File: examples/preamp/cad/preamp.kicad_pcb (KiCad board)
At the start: 2 copper layers, 52 parts, among them CON1 AVR-ISP-10, J1 CONN_01X02, J2 Conn_01x04, J3 CONN_01X03, J4 CONN_01X02, J5 CONN_01X03, J6 CONN_01X07, J7 CONN_01X02, J8 CONN_01X08, J9 CONN_01X08, Q1 ., SW1 Rotary_Encoder, SW2 SW_Push_Dual, SW3 SW_Push_Dual, SW4 SW_Push_Dual, SW5 SW_Push_Dual, U1 ATMEGA8A-PU, U2 DS1307+, U3 LM7809CT, U4 TDA7313, Y1 Crystal

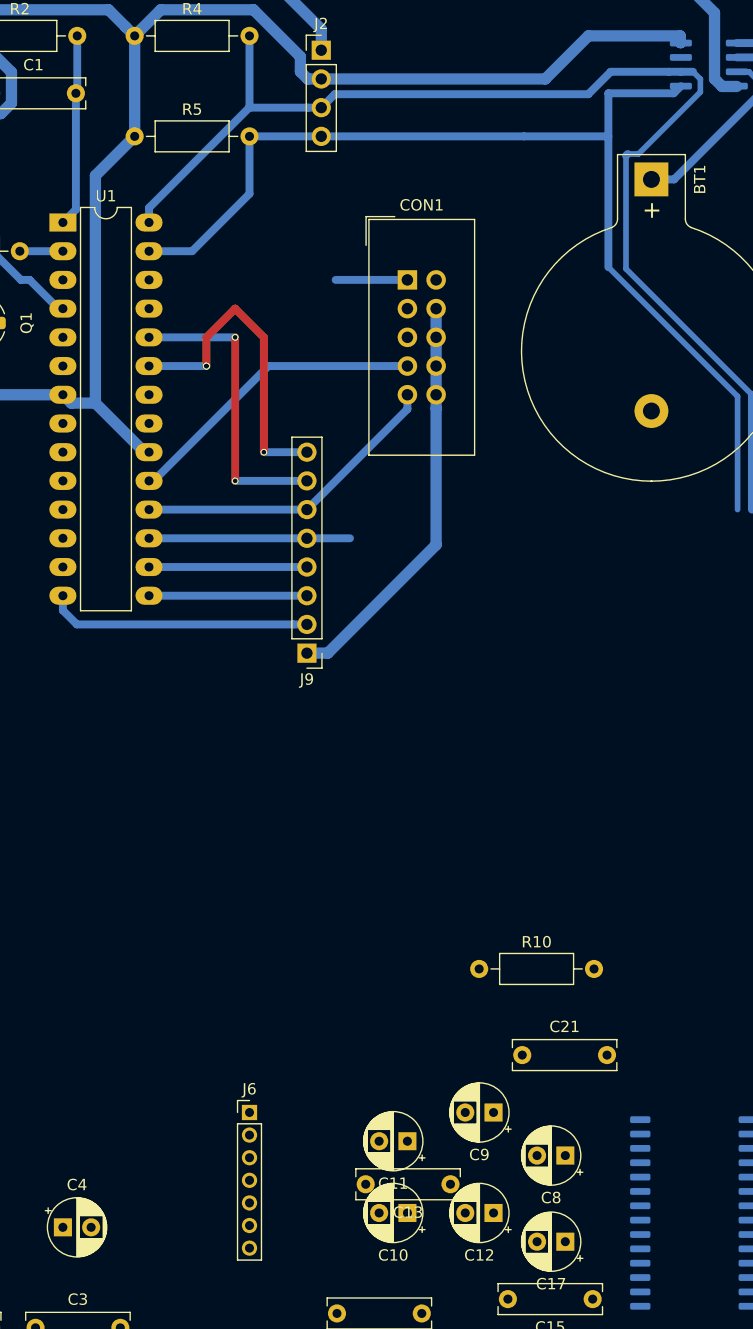
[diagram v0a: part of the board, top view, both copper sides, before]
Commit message: Rename kicad project
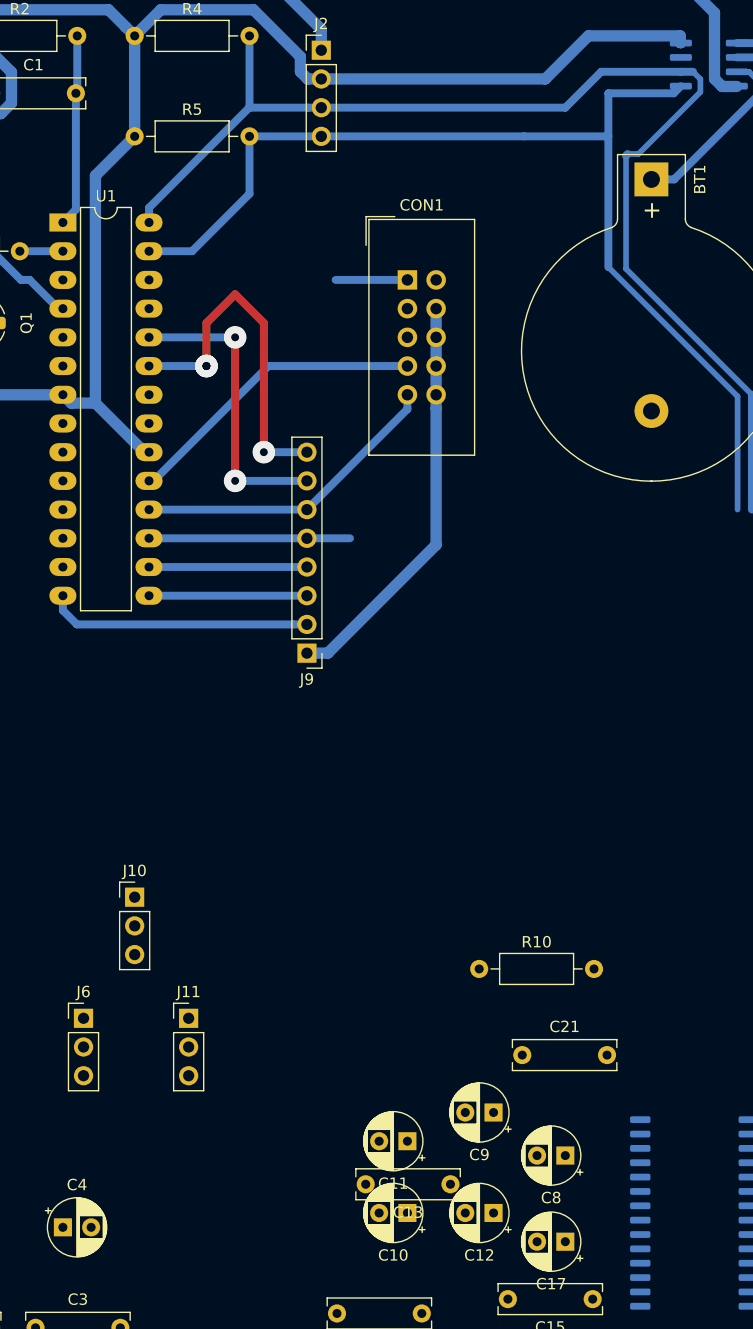
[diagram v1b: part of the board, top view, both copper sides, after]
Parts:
- added J10: Conn_01x03, Connector_PinHeader_2.54mm:PinHeader_1x03_P2.54mm_Vertical, F.Cu at (48.3, 96.5)
- added J11: Conn_01x03, Connector_PinHeader_2.54mm:PinHeader_1x03_P2.54mm_Vertical, F.Cu at (53.0, 107.2)
- J6: value CONN_01X07 -> Conn_01x03; footprint Connector_PinHeader_2.00mm:PinHeader_1x07_P2.00mm_Vertical -> Connector_PinHeader_2.54mm:PinHeader_1x03_P2.54mm_Vertical
- moved J6 16.9 mm to (43.7, 107.2)
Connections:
- J6 pad 2: Net-(C12-Pad2) -> Net-(C8-Pad2)
- J6 pad 3: Net-(C11-Pad2) -> Net-(C7-Pad2)
- U1 pad 25: Net-(U1-Pad25) -> /LEFT
- U1 pad 26: Net-(U1-Pad26) -> /RIGHT
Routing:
- net /ENC0: track 28.8 -> 31.3 mm
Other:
- net class Default: via_dia 0.6 -> 2; via_drill 0.4 -> 0.7
- net class power: via_dia 1 -> 2; via_drill 0.4 -> 0.7

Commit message: Update kicad project
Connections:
- U1 pad 11: Net-(U1-Pad11) -> /ENC1
- U1 pad 23: /ENC0 -> Net-(U1-Pad23)
- U1 pad 24: /ENC1 -> Net-(U1-Pad24)
- U1 pad 6: Net-(U1-Pad6) -> /ENC0
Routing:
- net /ENC0: track 31.3 -> 0.00 mm, vias 3 -> 0
- net /ENC1: track 26.7 -> 0.00 mm, vias 2 -> 0
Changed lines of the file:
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@@
     (thickness 1.6)
     (drawings 0)
-    (tracks 164)
+    (tracks 142)
     (zones 0)
     (modules 54)
@@
   (net 60 "Net-(U1-Pad3)")
   (net 61 "Net-(U1-Pad5)")
-  (net 62 "Net-(U1-Pad6)")
-  (net 63 "Net-(U1-Pad9)")
-  (net 64 "Net-(U1-Pad10)")
-  (net 65 "Net-(U1-Pad11)")
-  (net 66 "Net-(U1-Pad12)")
-  (net 67 "Net-(U1-Pad13)")
-  (net 68 "Net-(U2-Pad1)")
-  (net 69 "Net-(U2-Pad2)")
-  (net 70 "Net-(U2-Pad7)")
-  (net 71 "Net-(U4-Pad22)")
-  (net 72 "Net-(U4-Pad23)")
+  (net 62 "Net-(U1-Pad9)")
+  (net 63 "Net-(U1-Pad10)")
+  (net 64 "Net-(U1-Pad12)")
+  (net 65 "Net-(U1-Pad13)")
+  (net 66 "Net-(U2-Pad1)")
+  (net 67 "Net-(U2-Pad2)")
+  (net 68 "Net-(U2-Pad7)")
+  (net 69 "Net-(U4-Pad22)")
+  (net 70 "Net-(U4-Pad23)")
+  (net 71 "Net-(U1-Pad23)")
+  (net 72 "Net-(U1-Pad24)")
   (net_class Default "Это класс цепей по умолчанию."
     (clearance 0.5)
@@
     (add_net "Net-(Q1-Pad1)")
     (add_net "Net-(U1-Pad10)")
-    (add_net "Net-(U1-Pad11)")
     (add_net "Net-(U1-Pad12)")
     (add_net "Net-(U1-Pad13)")
+    (add_net "Net-(U1-Pad23)")
+    (add_net "Net-(U1-Pad24)")
     (add_net "Net-(U1-Pad3)")
     (add_net "Net-(U1-Pad5)")
-    (add_net "Net-(U1-Pad6)")
     (add_net "Net-(U1-Pad9)")
     (add_net "Net-(U2-Pad1)")
@@
     )
     (pad 1 smd roundrect (at -2.475 1.905 180) (size 1.95 0.6) (layers B.Cu B.Paste B.Mask) (roundrect_rratio 0.25)
-      (net 68 "Net-(U2-Pad1)"))
+      (net 66 "Net-(U2-Pad1)"))
     (pad 2 smd roundrect (at -2.475 0.635 180) (size 1.95 0.6) (layers B.Cu B.Paste B.Mask) (roundrect_rratio 0.25)
-      (net 69 "Net-(U2-Pad2)"))
+      (net 67 "Net-(U2-Pad2)"))
     (pad 3 smd roundrect (at -2.475 -0.635 180) (size 1.95 0.6) (layers B.Cu B.Paste B.Mask) (roundrect_rratio 0.25)
       (net 1 "Net-(BT1-Pad1)"))
@@
       (net 40 /SCL))
     (pad 7 smd roundrect (at 2.475 0.635 180) (size 1.95 0.6) (layers B.Cu B.Paste B.Mask) (roundrect_rratio 0.25)
-      (net 70 "Net-(U2-Pad7)"))
+      (net 68 "Net-(U2-Pad7)"))
     (pad 8 smd roundrect (at 2.475 1.905 180) (size 1.95 0.6) (layers B.Cu B.Paste B.Mask) (roundrect_rratio 0.25)
       (net 4 VCC))
@@
       (net 29 "Net-(C19-Pad2)"))
     (pad 22 smd roundrect (at 4.8 0.635) (size 1.8 0.6) (layers B.Cu B.Paste B.Mask) (roundrect_rratio 0.25)
-      (net 71 "Net-(U4-Pad22)"))
+      (net 69 "Net-(U4-Pad22)"))
     (pad 23 smd roundrect (at 4.8 1.905) (size 1.8 0.6) (layers B.Cu B.Paste B.Mask) (roundrect_rratio 0.25)
-      (net 72 "Net-(U4-Pad23)"))
+      (net 70 "Net-(U4-Pad23)"))
     (pad 24 smd roundrect (at 4.8 3.175) (size 1.8 0.6) (layers B.Cu B.Paste B.Mask) (roundrect_rratio 0.25)
       (net 43 /RIGHT))
@@
     (fp_line (start 3.6 -0.8) (end -1 -0.8) (layer F.CrtYd) (width 0.05))
     (pad 1 thru_hole circle (at 0 0) (size 1 1) (drill 0.5) (layers *.Cu *.Mask)
-      (net 68 "Net-(U2-Pad1)"))
+      (net 66 "Net-(U2-Pad1)"))
     (pad 2 thru_hole circle (at 2.54 0) (size 1 1) (drill 0.5) (layers *.Cu *.Mask)
-      (net 69 "Net-(U2-Pad2)"))
+      (net 67 "Net-(U2-Pad2)"))
     (model ${KISYS3DMOD}/Crystal.3dshapes/Crystal_AT310_D3.0mm_L10.0mm_Horizontal.wrl
       (at (xyz 0 0 0))
@@
       (net 37 /SCK))
     (pad 6 thru_hole oval (at 0 12.7) (size 2.4 1.6) (drill 0.8) (layers *.Cu *.Mask)
-      (net 62 "Net-(U1-Pad6)"))
+      (net 53 /ENC0))
     (pad 20 thru_hole oval (at 7.62 20.32) (size 2.4 1.6) (drill 0.8) (layers *.Cu *.Mask)
       (net 4 VCC))
@@
       (net 2 GND))
     (pad 9 thru_hole oval (at 0 20.32) (size 2.4 1.6) (drill 0.8) (layers *.Cu *.Mask)
-      (net 63 "Net-(U1-Pad9)"))
+      (net 62 "Net-(U1-Pad9)"))
     (pad 23 thru_hole oval (at 7.62 12.7) (size 2.4 1.6) (drill 0.8) (layers *.Cu *.Mask)
-      (net 53 /ENC0))
+      (net 71 "Net-(U1-Pad23)"))
     (pad 10 thru_hole oval (at 0 22.86) (size 2.4 1.6) (drill 0.8) (layers *.Cu *.Mask)
-      (net 64 "Net-(U1-Pad10)"))
+      (net 63 "Net-(U1-Pad10)"))
     (pad 24 thru_hole oval (at 7.62 10.16) (size 2.4 1.6) (drill 0.8) (layers *.Cu *.Mask)
-      (net 54 /ENC1))
+      (net 72 "Net-(U1-Pad24)"))
     (pad 11 thru_hole oval (at 0 25.4) (size 2.4 1.6) (drill 0.8) (layers *.Cu *.Mask)
-      (net 65 "Net-(U1-Pad11)"))
+      (net 54 /ENC1))
     (pad 25 thru_hole oval (at 7.62 7.62) (size 2.4 1.6) (drill 0.8) (layers *.Cu *.Mask)
       (net 44 /LEFT))
     (pad 12 thru_hole oval (at 0 27.94) (size 2.4 1.6) (drill 0.8) (layers *.Cu *.Mask)
-      (net 66 "Net-(U1-Pad12)"))
+      (net 64 "Net-(U1-Pad12)"))
     (pad 26 thru_hole oval (at 7.62 5.08) (size 2.4 1.6) (drill 0.8) (layers *.Cu *.Mask)
       (net 43 /RIGHT))
     (pad 13 thru_hole oval (at 0 30.48) (size 2.4 1.6) (drill 0.8) (layers *.Cu *.Mask)
-      (net 67 "Net-(U1-Pad13)"))
+      (net 65 "Net-(U1-Pad13)"))
     (pad 27 thru_hole oval (at 7.62 2.54) (size 2.4 1.6) (drill 0.8) (layers *.Cu *.Mask)
       (net 41 /SDA))
@@
   (segment (start 41.91 44.45) (end 41.51 44.45) (width 0.7) (layer B.Cu) (net 42))
   (segment (start 38.197998 41.91) (end 33.265998 36.978) (width 0.7) (layer B.Cu) (net 42))
-  (segment (start 49.53 49.53) (end 54.61 49.53) (width 0.7) (layer B.Cu) (net 53))
-  (segment (start 54.61 49.53) (end 54.61 49.53) (width 0.7) (layer B.Cu) (net 53))
-  (via (at 54.61 49.53) (size 2) (drill 0.7) (layers F.Cu B.Cu) (net 53))
-  (segment (start 54.61 49.53) (end 54.61 49.53) (width 0.7) (layer B.Cu) (net 53))
-  (via (at 54.61 49.53) (size 2) (drill 0.7) (layers F.Cu B.Cu) (net 53))
-  (segment (start 54.61 49.53) (end 54.61 46.99) (width 0.7) (layer F.Cu) (net 53))
-  (segment (start 54.61 45.72) (end 57.15 43.18) (width 0.7) (layer F.Cu) (net 53))
-  (segment (start 57.15 43.18) (end 59.69 45.72) (width 0.7) (layer F.Cu) (net 53))
-  (segment (start 59.69 46.99) (end 59.69 57.15) (width 0.7) (layer F.Cu) (net 53))
-  (segment (start 59.69 57.15) (end 59.69 57.15) (width 0.7) (layer F.Cu) (net 53))
-  (via (at 59.69 57.15) (size 2) (drill 0.7) (layers F.Cu B.Cu) (net 53))
-  (segment (start 63.5 57.15) (end 59.69 57.15) (width 0.7) (layer B.Cu) (net 53))
-  (segment (start 59.69 45.72) (end 59.69 46.99) (width 0.7) (layer F.Cu) (net 53))
-  (segment (start 54.61 45.72) (end 54.61 46.99) (width 0.7) (layer F.Cu) (net 53))
-  (segment (start 49.53 46.99) (end 57.15 46.99) (width 0.7) (layer B.Cu) (net 54))
-  (segment (start 57.15 46.99) (end 57.15 46.99) (width 0.7) (layer B.Cu) (net 54))
-  (segment (start 57.15 46.99) (end 57.15 46.99) (width 0.7) (layer F.Cu) (net 54))
-  (segment (start 57.15 59.69) (end 57.15 59.69) (width 0.7) (layer F.Cu) (net 54))
-  (via (at 57.15 59.69) (size 2) (drill 0.7) (layers F.Cu B.Cu) (net 54))
-  (segment (start 57.15 59.69) (end 63.5 59.69) (width 0.7) (layer B.Cu) (net 54))
-  (segment (start 57.15 46.99) (end 57.15 59.69) (width 0.7) (layer F.Cu) (net 54))
-  (via (at 57.15 46.99) (size 2) (drill 0.7) (layers F.Cu B.Cu) (net 54))
   (segment (start 49.53 67.31) (end 63.5 67.31) (width 0.7) (layer B.Cu) (net 55))
   (segment (start 49.53 69.85) (end 63.5 69.85) (width 0.7) (layer B.Cu) (net 56))
@@
   (segment (start 27.94 39.37) (end 29.21 39.37) (width 0.7) (layer B.Cu) (net 58))
   (segment (start 38.1 39.37) (end 41.91 39.37) (width 0.7) (layer B.Cu) (net 59))
-  (segment (start 106.045 20.955) (end 106.68 21.59) (width 0.7) (layer B.Cu) (net 68))
-  (segment (start 101.535 20.955) (end 106.045 20.955) (width 0.7) (layer B.Cu) (net 68))
-  (segment (start 108.720001 22.089999) (end 109.22 21.59) (width 0.7) (layer B.Cu) (net 69))
-  (segment (start 105.464998 22.225) (end 106.079999 22.840001) (width 0.5) (layer B.Cu) (net 69))
-  (segment (start 107.969999 22.840001) (end 108.720001 22.089999) (width 0.7) (layer B.Cu) (net 69))
-  (segment (start 106.079999 22.840001) (end 107.969999 22.840001) (width 0.5) (layer B.Cu) (net 69))
-  (segment (start 101.535 22.225) (end 105.464998 22.225) (width 0.7) (layer B.Cu) (net 69))
+  (segment (start 106.045 20.955) (end 106.68 21.59) (width 0.7) (layer B.Cu) (net 66))
+  (segment (start 101.535 20.955) (end 106.045 20.955) (width 0.7) (layer B.Cu) (net 66))
+  (segment (start 108.720001 22.089999) (end 109.22 21.59) (width 0.7) (layer B.Cu) (net 67))
+  (segment (start 105.464998 22.225) (end 106.079999 22.840001) (width 0.5) (layer B.Cu) (net 67))
+  (segment (start 107.969999 22.840001) (end 108.720001 22.089999) (width 0.7) (layer B.Cu) (net 67))
+  (segment (start 106.079999 22.840001) (end 107.969999 22.840001) (width 0.5) (layer B.Cu) (net 67))
+  (segment (start 101.535 22.225) (end 105.464998 22.225) (width 0.7) (layer B.Cu) (net 67))
   (zone (net 2) (net_name GND) (layer B.Cu) (hatch edge 0.508)
     (connect_pads (clearance 0.508))

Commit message: Update preamp scheme
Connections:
- J2 pad 3: /SCL -> /SDA
- J2 pad 4: /SDA -> /SCL
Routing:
- net GND: track 183.5 -> 0.00 mm
- net VCC: track 176.2 -> 0.00 mm
- net /SCL: track 107.7 -> 0.00 mm
- net /SDA: track 96.1 -> 0.00 mm
- net /PowerBTN_MISO: track 27.8 -> 0.00 mm
- net /SCK: track 27.1 -> 0.00 mm
- net /IRint: track 26.4 -> 0.00 mm
- net /BTN3_MOSI: track 24.1 -> 0.00 mm
- net /BTN0: track 23.4 -> 0.00 mm
- net Net-(D1-Pad2): track 21.9 -> 0.00 mm
- net /Reset: track 17.0 -> 0.00 mm
- net Net-(BT1-Pad1): track 15.9 -> 0.00 mm
- net /BTN2: track 14.0 -> 0.00 mm
- net /BTN1: track 14.0 -> 0.00 mm
- net Net-(U2-Pad2): track 8.46 -> 0.00 mm
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- removed copper zone on B.Cu, net GND

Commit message: Update preamp scheme
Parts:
- removed D1: D, Diode_THT:D_T-1_P10.16mm_Horizontal
- removed the J7 at (20.3, 55.9)
- removed the J8 at (153.7, 61.0)
- removed the J9 at (63.5, 74.9)
- removed SW1: Rotary_Encoder, Rotary_Encoder:RotaryEncoder_Alps_EC11E-Switch_Vertical_H20mm
- removed SW2, SW3, SW4, SW5: SW_Push_Dual, Button_Switch_THT:SW_PUSH_6mm
- added J2: Conn_01x03, Connector_PinHeader_2.54mm:PinHeader_1x03_P2.54mm_Vertical, F.Cu at (125.6, 69.1)
- added J3: Conn_01x03, Connector_PinHeader_2.54mm:PinHeader_1x03_P2.54mm_Vertical, F.Cu at (117.0, 73.2)
- added J4: Conn_01x03, Connector_PinHeader_2.54mm:PinHeader_1x03_P2.54mm_Vertical, F.Cu at (130.3, 69.1)
- added J5: Conn_01x03, Connector_PinHeader_2.54mm:PinHeader_1x03_P2.54mm_Vertical, F.Cu at (134.9, 69.1)
- added J6: Conn_01x03, Connector_PinHeader_2.54mm:PinHeader_1x03_P2.54mm_Vertical, F.Cu at (139.6, 69.1)
- added Q2: ., Package_TO_SOT_THT:TO-92_HandSolder, F.Cu at (121.3, 80.1)
- added R2: 10k, Resistor_THT:R_Axial_DIN0207_L6.3mm_D2.5mm_P10.16mm_Horizontal, F.Cu at (111.6, 68.8)
- J1: value CONN_01X02 -> Conn_01x04; footprint Connector_PinHeader_2.54mm:PinHeader_1x02_P2.54mm_Vertical -> Connector_PinHeader_2.54mm:PinHeader_1x04_P2.54mm_Vertical
- R1: renamed from R9; value 3k -> 10k
- R6: renamed from R8; value 5.5k -> 5.6k
- R7: renamed from R10; value 5.5k -> 5.6k
- moved J1 98.2 mm to (112.3, 73.2)
- renumbered C2 to C1, C14 to C10, C17 to C11, C4 to C12, C5 to C13, C23 to C14, C6 to C15, C13 to C16, C16 to C17, C19 to C18, C21 to C19, C1 to C2, C15 to C20, C18 to C21, C20 to C22, C22 to C23, C7 to C3, C9 to C4, C11 to C5, C8 to C6, C10 to C7, C3 to C8, C12 to C9, J4 to J12, J5 to J13, J2 to J7, J3 to J8, J6 to J9, R4 to R3, R5 to R4, R2 to R5
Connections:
- CON1 pad 2: VCC -> Net-(CON1-Pad2)
- J1 pad 2: VCC -> /BTN2
- U1 pad 12: Net-(U1-Pad12) -> /Power
- U1 pad 2: /Power -> Net-(U1-Pad2)

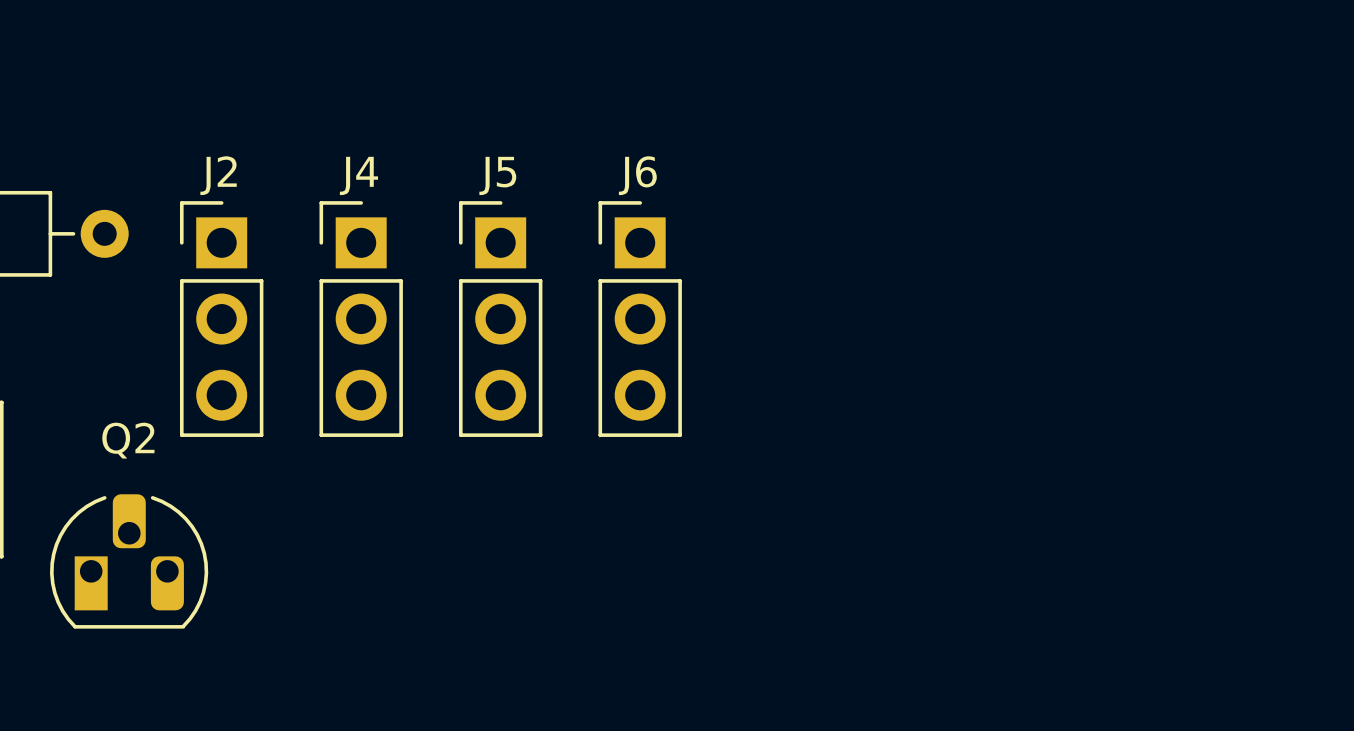
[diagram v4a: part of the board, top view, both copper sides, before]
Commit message: Add 3 Input buttons
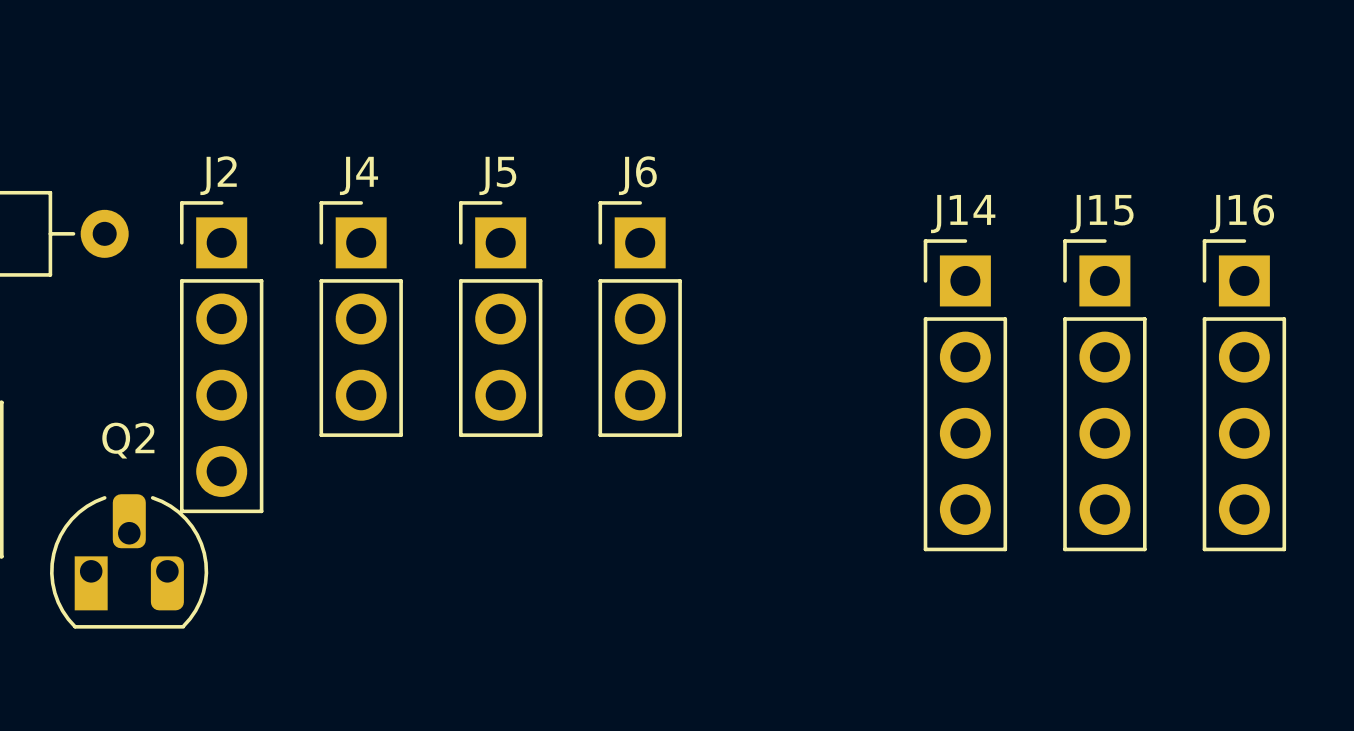
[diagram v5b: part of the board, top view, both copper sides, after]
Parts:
- added J14: Conn_01x04, Connector_PinHeader_2.54mm:PinHeader_1x04_P2.54mm_Vertical, F.Cu at (150.4, 70.4)
- added J15: Conn_01x04, Connector_PinHeader_2.54mm:PinHeader_1x04_P2.54mm_Vertical, F.Cu at (155.1, 70.4)
- added J16: Conn_01x04, Connector_PinHeader_2.54mm:PinHeader_1x04_P2.54mm_Vertical, F.Cu at (159.7, 70.4)
- J2: value Conn_01x03 -> Conn_01x04; footprint Connector_PinHeader_2.54mm:PinHeader_1x03_P2.54mm_Vertical -> Connector_PinHeader_2.54mm:PinHeader_1x04_P2.54mm_Vertical
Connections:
- U1 pad 13: Net-(U1-Pad13) -> /Input3Led
- U1 pad 23: Net-(U1-Pad23) -> /Input1Led
- U1 pad 24: Net-(U1-Pad24) -> /Input2Led
